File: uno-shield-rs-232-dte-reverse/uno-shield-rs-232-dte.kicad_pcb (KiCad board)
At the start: 2 copper layers, 68.6 x 53.3 mm, 22 parts, among them J1 Ctrl Route, J3 DSR/CTS, J4 DB9_Male, P1 Power, P2 Analog, P3 Digital, P4 Digital, P5 CONN_01X01, P6 CONN_01X01, P7 CONN_01X01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

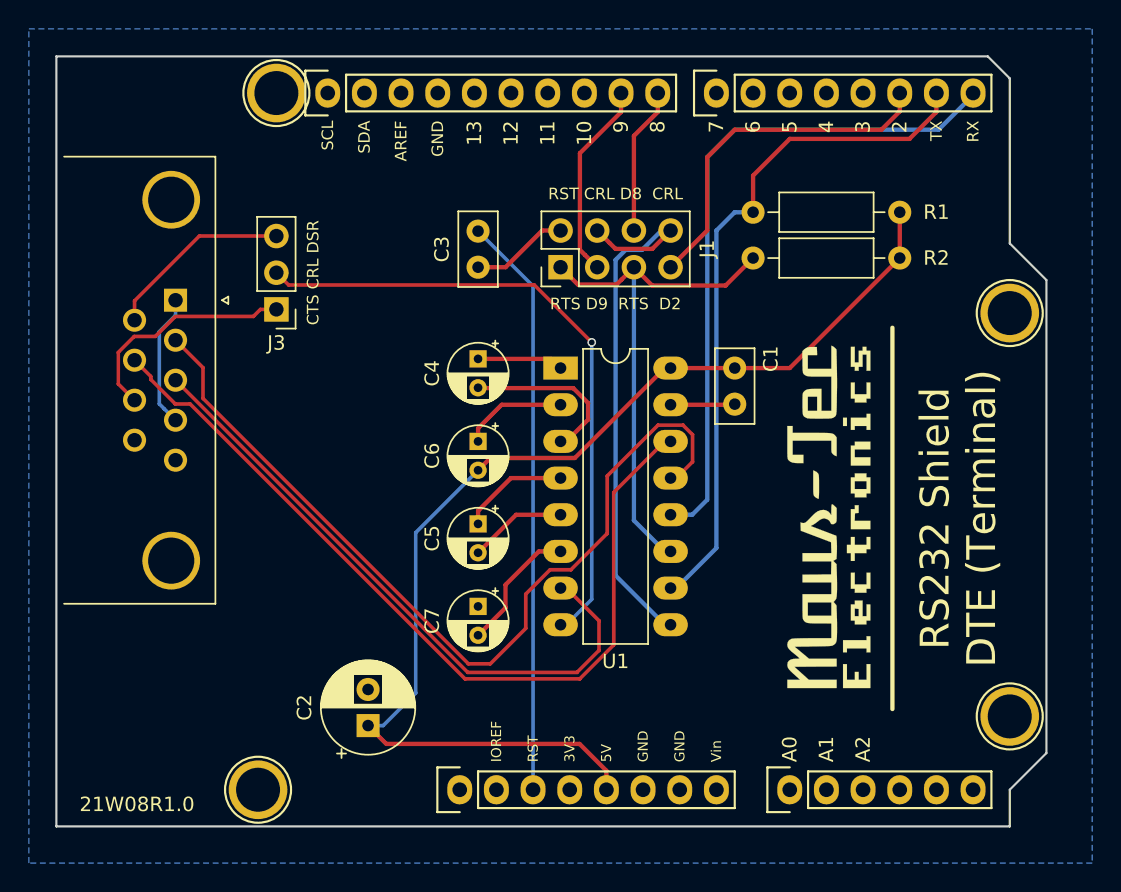
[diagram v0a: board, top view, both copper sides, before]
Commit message: Propagate signal routing changes to DTE-R shield.
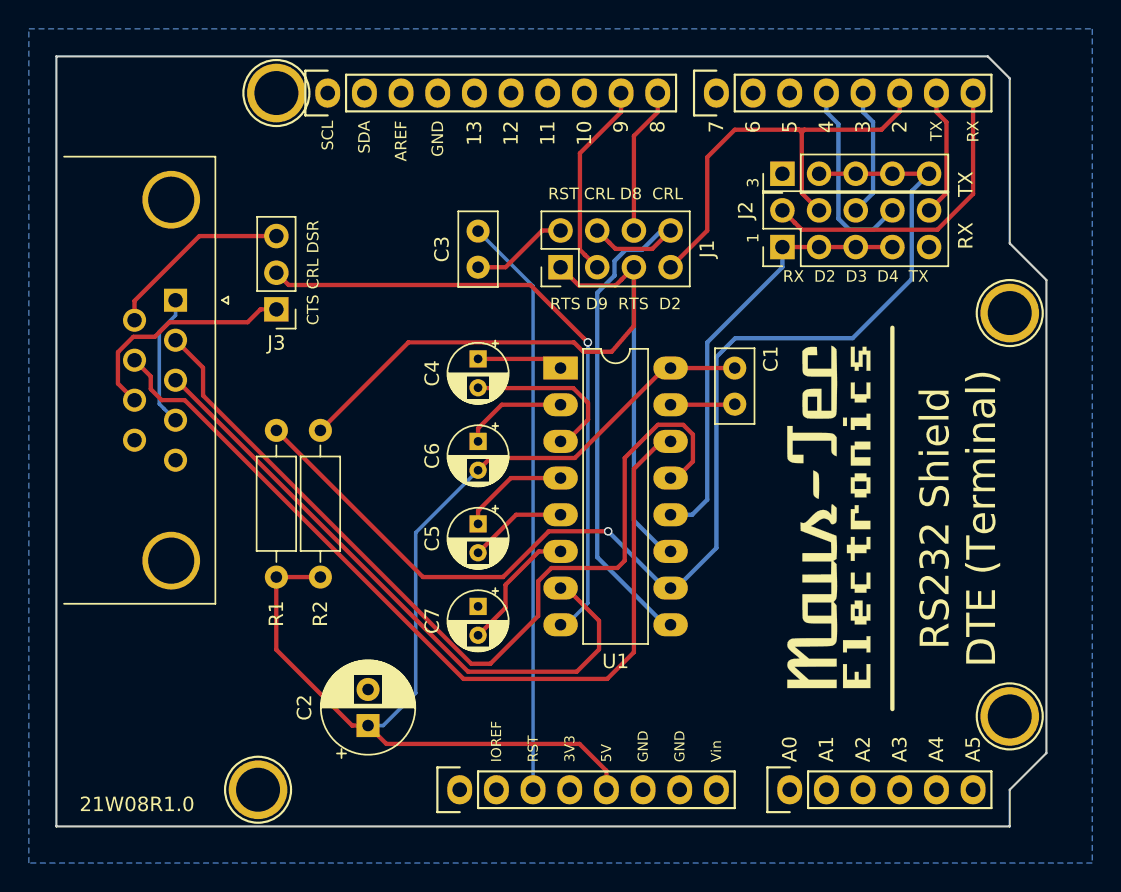
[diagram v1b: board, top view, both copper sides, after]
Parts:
- added J2: RX Route, Connector_PinHeader_2.54mm:PinHeader_2x05_P2.54mm_Vertical, F.Cu at (161.3, 86.2)
- added J5: TX Route, Connector_PinHeader_2.54mm:PinHeader_1x05_P2.54mm_Vertical, F.Cu at (161.3, 81.2)
- moved R1 50.0 mm to (126.2, 109.1), turned to 90 degrees
- moved R2 45.8 mm to (129.3, 109.1), turned to 90 degrees
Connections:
- P4 pad 4: /4 -> D4
- P4 pad 5: /3(**) -> D3
- R1 pad 2: TX -> UTX
- U1 pad 10: TX -> UTX
- U1 pad 12: RX -> URX
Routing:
- net UTX: track 0.00 -> 83.2 mm, vias 0 -> 1
- net TX: track 47.8 -> 8.91 mm
- net URX: track 0.00 -> 30.2 mm
- net RX: track 47.0 -> 21.9 mm
- net /URTS: track 36.6 -> 56.5 mm
- net D4: track 0.00 -> 13.7 mm
- net D3: track 0.00 -> 8.91 mm
- net D2: track 24.6 -> 31.2 mm
- net /RTS: track 59.4 -> 61.4 mm
- net /RXD: track 61.1 -> 62.9 mm
- net +5V: track 79.1 -> 77.9 mm
- net /UCTRL: track 37.9 -> 38.9 mm
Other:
- board text added: "1 3"
- board text added: "A3"
- board text added: "A4"
- board text added: "A5"
- board text added: "RX D2 D3 D4 TX"
- board text added: "RX TX"
